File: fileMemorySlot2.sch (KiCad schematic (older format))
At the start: 4 parts, among them J13 MM1_addressExtension, J8 MM1_receptacle_5530843-2

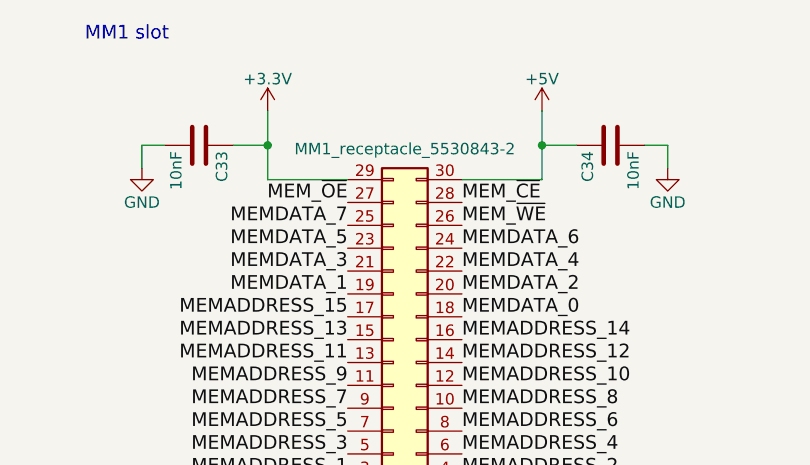
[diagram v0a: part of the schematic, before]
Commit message: Better decoupling
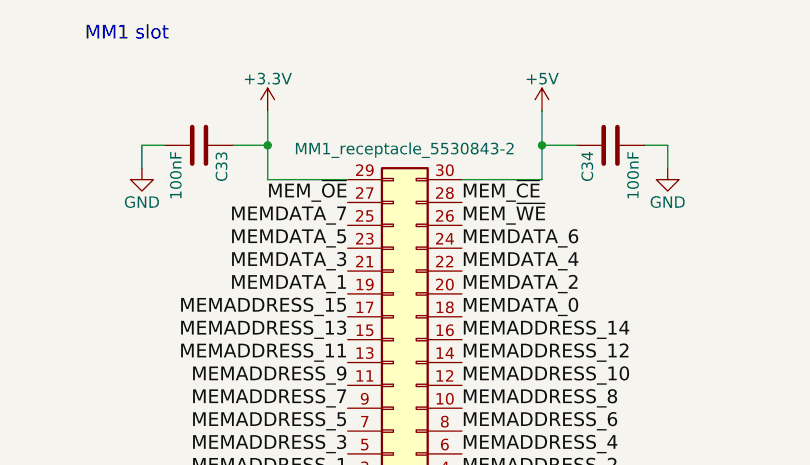
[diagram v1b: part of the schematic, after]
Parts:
- C26, C27: value 10nF -> 100nF
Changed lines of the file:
@@
 AR Path="/5E0692F0/5BB77E95" Ref="C33"  Part="1"
 F 0 "C33" H 5275 1750 50  0000 L CNN
-F 1 "10nF" H 5275 1550 50  0000 L CNN
+F 1 "100nF" H 5275 1550 50  0000 L CNN
 F 2 "Capacitor_SMD:C_0805_2012Metric" H 5288 1500 50  0001 C CNN
 F 3 "" H 5250 1650 50  0001 C CNN
@@
 AR Path="/5E0692F0/5BB77E9C" Ref="C34"  Part="1"
 F 0 "C34" H 7075 1750 50  0000 L CNN
-F 1 "10nF" H 7075 1550 50  0000 L CNN
+F 1 "100nF" H 7075 1550 50  0000 L CNN
 F 2 "Capacitor_SMD:C_0805_2012Metric" H 7088 1500 50  0001 C CNN
 F 3 "" H 7050 1650 50  0001 C CNN
